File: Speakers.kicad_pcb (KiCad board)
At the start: 2 copper layers, 58.4 x 83.6 mm, 16 parts, among them J1 SR, J2 SL, J3 SAR, J4 SAL, J5 SBR, J6 SBL, J7 5V, Q1 S8050, Q2 S8050, U1 WeMos_mini

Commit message: Zmiana wartości R1 i R2
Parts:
- R1, R2: value 1k -> 1k8
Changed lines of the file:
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@@
       (effects (font (size 1 1) (thickness 0.15)) (justify mirror))
     )
-    (fp_text value 1k (at 0 -1.9 270) (layer B.Fab)
+    (fp_text value 1k8 (at 0 -1.9 270) (layer B.Fab)
       (effects (font (size 1 1) (thickness 0.15)) (justify mirror))
     )
@@
       (effects (font (size 1 1) (thickness 0.15)) (justify mirror))
     )
-    (fp_text value 1k (at 0 -1.9) (layer B.Fab)
+    (fp_text value 1k8 (at 0 -1.9) (layer B.Fab)
       (effects (font (size 1 1) (thickness 0.15)) (justify mirror))
     )
@@
   (segment (start 249.428 116.586) (end 240.792 107.95) (width 1.5) (layer B.Cu) (net 14))
   (segment (start 249.428 124.968) (end 249.428 116.586) (width 1.5) (layer B.Cu) (net 14))
-  (segment (start 228.092 103.632) (end 226.79 103.632) (width 1.5) (layer B.Cu) (net 14) (status 800000))
+  (segment (start 228.092 103.632) (end 226.79 103.632) (width 1.5) (layer B.Cu) (net 14))
   (segment (start 232.41 107.95) (end 228.092 103.632) (width 1.5) (layer B.Cu) (net 14))
-  (segment (start 230.312 97.766) (end 232.608 97.766) (width 1.5) (layer B.Cu) (net 15) (status C00000))
-  (segment (start 232.608 97.766) (end 232.664 97.822) (width 1.5) (layer B.Cu) (net 15) (status C00000))
+  (segment (start 230.312 97.766) (end 232.608 97.766) (width 1.5) (layer B.Cu) (net 15))
+  (segment (start 232.608 97.766) (end 232.664 97.822) (width 1.5) (layer B.Cu) (net 15))
   (segment (start 222.504 102.394) (end 222.504 98.552) (width 1.5) (layer B.Cu) (net 16))
   (segment (start 222.504 98.552) (end 222.25 98.298) (width 1.5) (layer B.Cu) (net 16))

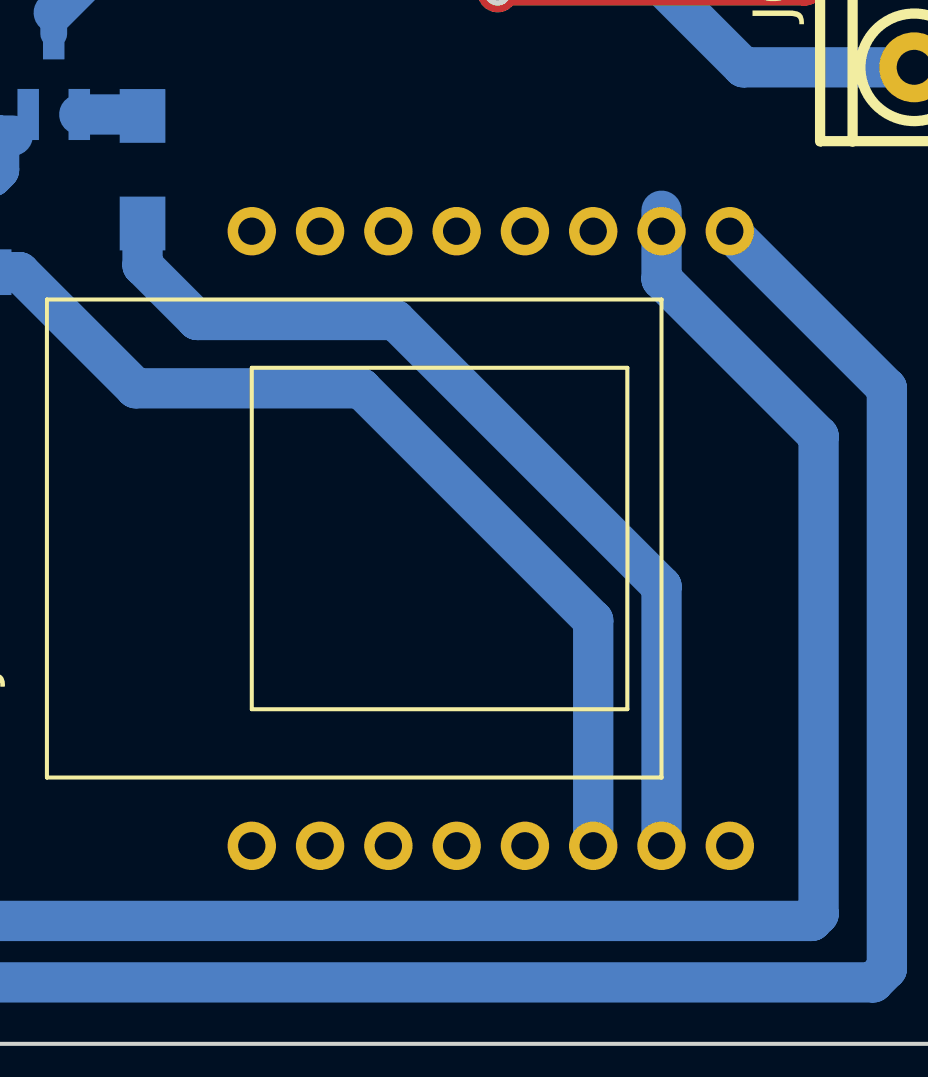
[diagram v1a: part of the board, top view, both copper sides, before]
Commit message: dodano plik pdf z PCB
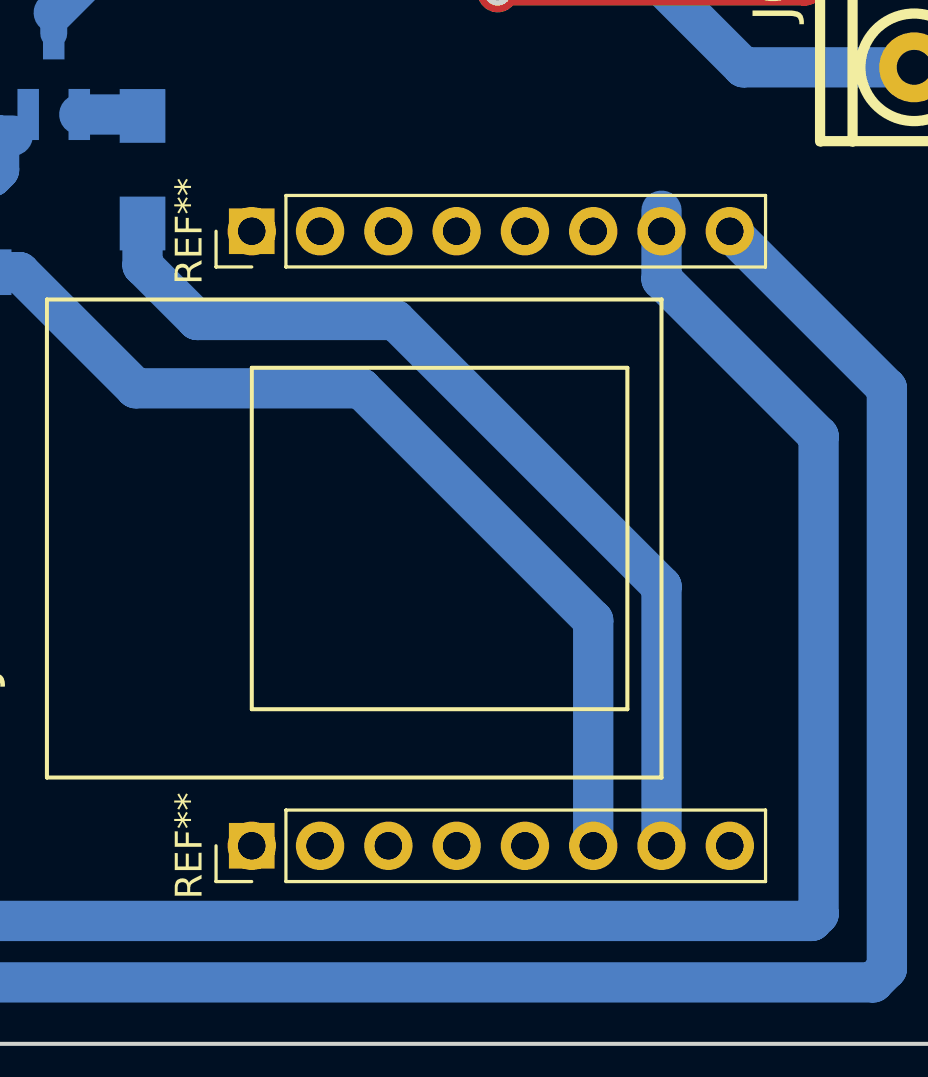
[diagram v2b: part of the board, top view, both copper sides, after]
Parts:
- added REF**: Socket_Strip_Straight_1x08_Pitch2.54mm, Socket_Strips:Socket_Strip_Straight_1x08_Pitch2.54mm, F.Cu at (236.7, 102.1)
- added REF**: Socket_Strip_Straight_1x08_Pitch2.54mm, Socket_Strips:Socket_Strip_Straight_1x08_Pitch2.54mm, F.Cu at (236.7, 125.0)
- R1, R2: value 1k8 -> 1k
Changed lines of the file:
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@@
-(kicad_pcb (version 4) (host pcbnew 4.0.7-e1-6374~58~ubuntu16.04.1)
+(kicad_pcb (version 4) (host pcbnew 4.0.7+dfsg1-1ubuntu2)
   (general
-    (links 30)
+    (links 0)
     (no_connects 2)
     (area 212.776999 48.692999 271.347001 132.409001)
@@
     (tracks 154)
     (zones 0)
-    (modules 16)
+    (modules 18)
     (nets 17)
   )
@@
     (pad_to_mask_clearance 0.2)
     (aux_axis_origin 0 0)
-    (visible_elements 7FFFFFFF)
+    (visible_elements 7FFFEFFF)
     (pcbplotparams
       (layerselection 0x00030_80000001)
@@
     (pad 14 thru_hole circle (at 25.32 0) (size 3 3) (drill 1.3) (layers *.Cu *.Mask)
       (net 7 "Net-(J5-Pad1)"))
-    (model ${KISYS3DMOD}/Relays_THT.3dshapes/Relay_DPDT_Finder_40.52.wrl
-      (at (xyz 0 0 0))
-      (scale (xyz 1 1 1))
-      (rotate (xyz 0 0 0))
+    (model Relays_THT.3dshapes/Rely_RM84.wrl
+      (at (xyz 1.06 0.1 0))
+      (scale (xyz 0.4 0.4 0.4))
+      (rotate (xyz 0 0 180))
     )
   )
@@
     (pad 14 thru_hole circle (at 25.32 0) (size 3 3) (drill 1.3) (layers *.Cu *.Mask)
       (net 7 "Net-(J5-Pad1)"))
-    (model ${KISYS3DMOD}/Relays_THT.3dshapes/Relay_DPDT_Finder_40.52.wrl
-      (at (xyz 0 0 0))
-      (scale (xyz 1 1 1))
-      (rotate (xyz 0 0 0))
+    (model Relays_THT.3dshapes/Rely_RM84.wrl
+      (at (xyz 1.06 0.1 0))
+      (scale (xyz 0.4 0.4 0.4))
+      (rotate (xyz 0 0 180))
     )
   )
@@
       (effects (font (size 1 1) (thickness 0.15)) (justify mirror))
     )
-    (fp_text value 1k8 (at 0 -1.9 270) (layer B.Fab)
+    (fp_text value 1k (at 0 -1.9 270) (layer B.Fab)
       (effects (font (size 1 1) (thickness 0.15)) (justify mirror))
     )
@@
       (effects (font (size 1 1) (thickness 0.15)) (justify mirror))
     )
-    (fp_text value 1k8 (at 0 -1.9) (layer B.Fab)
+    (fp_text value 1k (at 0 -1.9) (layer B.Fab)
       (effects (font (size 1 1) (thickness 0.15)) (justify mirror))
     )
@@
     )
   )
+  (module Socket_Strips:Socket_Strip_Straight_1x08_Pitch2.54mm (layer F.Cu)
+    (at 236.728 102.108 90)
+    (descr "Through hole straight socket strip, 1x08, 2.54mm pitch, single row")
+    (tags "Through hole socket strip THT 1x08 2.54mm single row")
+    (fp_text reference REF** (at 0 -2.33 90) (layer F.SilkS)
+      (effects (font (size 1 1) (thickness 0.15)))
+    )
+    (fp_text value Socket_Strip_Straight_1x08_Pitch2.54mm (at 0 20.11 90) (layer F.Fab)
+      (effects (font (size 1 1) (thickness 0.15)))
+    )
+    (fp_line (start -1.27 -1.27) (end -1.27 19.05) (layer F.Fab) (width 0.1))
+    (fp_line (start -1.27 19.05) (end 1.27 19.05) (layer F.Fab) (width 0.1))
+    (fp_line (start 1.27 19.05) (end 1.27 -1.27) (layer F.Fab) (width 0.1))
+    (fp_line (start 1.27 -1.27) (end -1.27 -1.27) (layer F.Fab) (width 0.1))
+    (fp_line (start -1.33 1.27) (end -1.33 19.11) (layer F.SilkS) (width 0.12))
+    (fp_line (start -1.33 19.11) (end 1.33 19.11) (layer F.SilkS) (width 0.12))
+    (fp_line (start 1.33 19.11) (end 1.33 1.27) (layer F.SilkS) (width 0.12))
+    (fp_line (start 1.33 1.27) (end -1.33 1.27) (layer F.SilkS) (width 0.12))
+    (fp_line (start -1.33 0) (end -1.33 -1.33) (layer F.SilkS) (width 0.12))
+    (fp_line (start -1.33 -1.33) (end 0 -1.33) (layer F.SilkS) (width 0.12))
+    (fp_line (start -1.8 -1.8) (end -1.8 19.55) (layer F.CrtYd) (width 0.05))
+    (fp_line (start -1.8 19.55) (end 1.8 19.55) (layer F.CrtYd) (width 0.05))
+    (fp_line (start 1.8 19.55) (end 1.8 -1.8) (layer F.CrtYd) (width 0.05))
+    (fp_line (start 1.8 -1.8) (end -1.8 -1.8) (layer F.CrtYd) (width 0.05))
+    (fp_text user %R (at 0 -2.33 90) (layer F.Fab)
+      (effects (font (size 1 1) (thickness 0.15)))
+    )
+    (pad 1 thru_hole rect (at 0 0 90) (size 1.7 1.7) (drill 1) (layers *.Cu *.Mask))
+    (pad 2 thru_hole oval (at 0 2.54 90) (size 1.7 1.7) (drill 1) (layers *.Cu *.Mask))
+    (pad 3 thru_hole oval (at 0 5.08 90) (size 1.7 1.7) (drill 1) (layers *.Cu *.Mask))
+    (pad 4 thru_hole oval (at 0 7.62 90) (size 1.7 1.7) (drill 1) (layers *.Cu *.Mask))
+    (pad 5 thru_hole oval (at 0 10.16 90) (size 1.7 1.7) (drill 1) (layers *.Cu *.Mask))
+    (pad 6 thru_hole oval (at 0 12.7 90) (size 1.7 1.7) (drill 1) (layers *.Cu *.Mask))
+    (pad 7 thru_hole oval (at 0 15.24 90) (size 1.7 1.7) (drill 1) (layers *.Cu *.Mask))
+    (pad 8 thru_hole oval (at 0 17.78 90) (size 1.7 1.7) (drill 1) (layers *.Cu *.Mask))
+    (model ${KISYS3DMOD}/Socket_Strips.3dshapes/Socket_Strip_Straight_1x08_Pitch2.54mm.wrl
+      (at (xyz 0 -0.35 0))
+      (scale (xyz 1 1 1))
+      (rotate (xyz 0 0 270))
+    )
+  )
+  (module Socket_Strips:Socket_Strip_Straight_1x08_Pitch2.54mm (layer F.Cu)
+    (at 236.728 124.968 90)
+    (descr "Through hole straight socket strip, 1x08, 2.54mm pitch, single row")
+    (tags "Through hole socket strip THT 1x08 2.54mm single row")
+    (fp_text reference REF** (at 0 -2.33 90) (layer F.SilkS)
+      (effects (font (size 1 1) (thickness 0.15)))
+    )
+    (fp_text value Socket_Strip_Straight_1x08_Pitch2.54mm (at 0 20.11 90) (layer F.Fab)
+      (effects (font (size 1 1) (thickness 0.15)))
+    )
+    (fp_line (start -1.27 -1.27) (end -1.27 19.05) (layer F.Fab) (width 0.1))
+    (fp_line (start -1.27 19.05) (end 1.27 19.05) (layer F.Fab) (width 0.1))
+    (fp_line (start 1.27 19.05) (end 1.27 -1.27) (layer F.Fab) (width 0.1))
+    (fp_line (start 1.27 -1.27) (end -1.27 -1.27) (layer F.Fab) (width 0.1))
+    (fp_line (start -1.33 1.27) (end -1.33 19.11) (layer F.SilkS) (width 0.12))
+    (fp_line (start -1.33 19.11) (end 1.33 19.11) (layer F.SilkS) (width 0.12))
+    (fp_line (start 1.33 19.11) (end 1.33 1.27) (layer F.SilkS) (width 0.12))
+    (fp_line (start 1.33 1.27) (end -1.33 1.27) (layer F.SilkS) (width 0.12))
+    (fp_line (start -1.33 0) (end -1.33 -1.33) (layer F.SilkS) (width 0.12))
+    (fp_line (start -1.33 -1.33) (end 0 -1.33) (layer F.SilkS) (width 0.12))
+    (fp_line (start -1.8 -1.8) (end -1.8 19.55) (layer F.CrtYd) (width 0.05))
+    (fp_line (start -1.8 19.55) (end 1.8 19.55) (layer F.CrtYd) (width 0.05))
+    (fp_line (start 1.8 19.55) (end 1.8 -1.8) (layer F.CrtYd) (width 0.05))
+    (fp_line (start 1.8 -1.8) (end -1.8 -1.8) (layer F.CrtYd) (width 0.05))
+    (fp_text user %R (at 0 -2.33 90) (layer F.Fab)
+      (effects (font (size 1 1) (thickness 0.15)))
+    )
+    (pad 1 thru_hole rect (at 0 0 90) (size 1.7 1.7) (drill 1) (layers *.Cu *.Mask))
+    (pad 2 thru_hole oval (at 0 2.54 90) (size 1.7 1.7) (drill 1) (layers *.Cu *.Mask))
+    (pad 3 thru_hole oval (at 0 5.08 90) (size 1.7 1.7) (drill 1) (layers *.Cu *.Mask))
+    (pad 4 thru_hole oval (at 0 7.62 90) (size 1.7 1.7) (drill 1) (layers *.Cu *.Mask))
+    (pad 5 thru_hole oval (at 0 10.16 90) (size 1.7 1.7) (drill 1) (layers *.Cu *.Mask))
+    (pad 6 thru_hole oval (at 0 12.7 90) (size 1.7 1.7) (drill 1) (layers *.Cu *.Mask))
+    (pad 7 thru_hole oval (at 0 15.24 90) (size 1.7 1.7) (drill 1) (layers *.Cu *.Mask))
+    (pad 8 thru_hole oval (at 0 17.78 90) (size 1.7 1.7) (drill 1) (layers *.Cu *.Mask))
+    (model ${KISYS3DMOD}/Socket_Strips.3dshapes/Socket_Strip_Straight_1x08_Pitch2.54mm.wrl
+      (at (xyz 0 -0.35 0))
+      (scale (xyz 1 1 1))
+      (rotate (xyz 0 0 270))
+    )
+  )

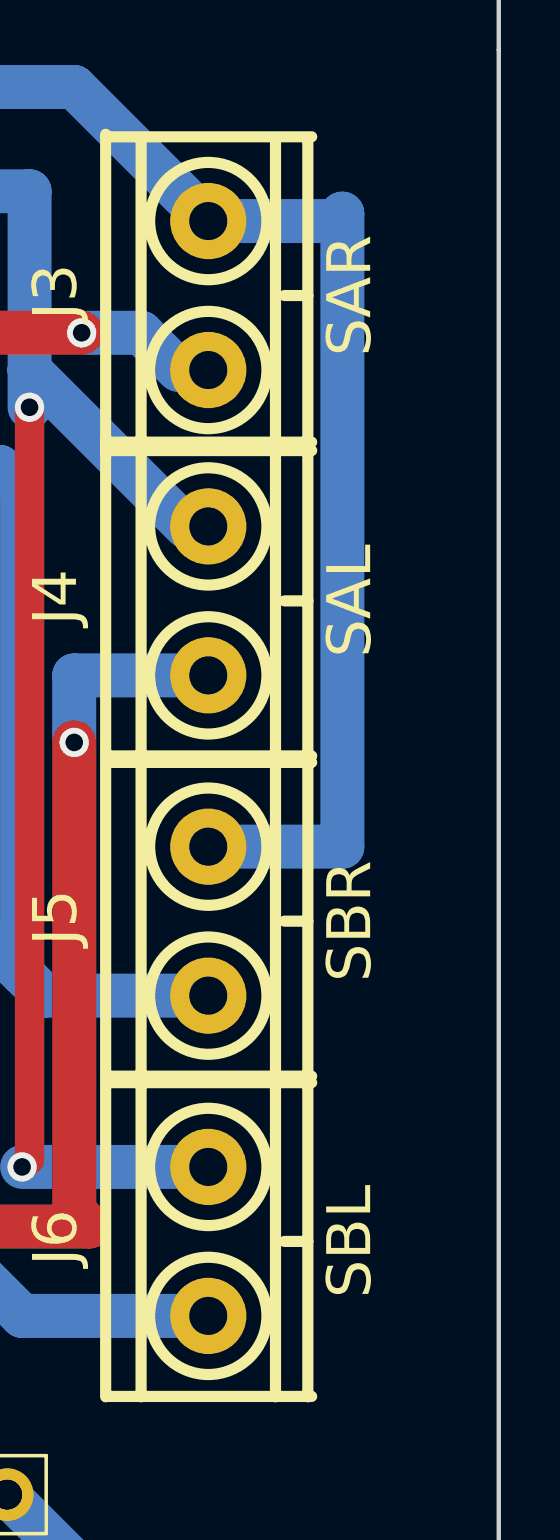
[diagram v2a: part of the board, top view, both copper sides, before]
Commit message: dodano opisy przy złączkach na warstwie górnej
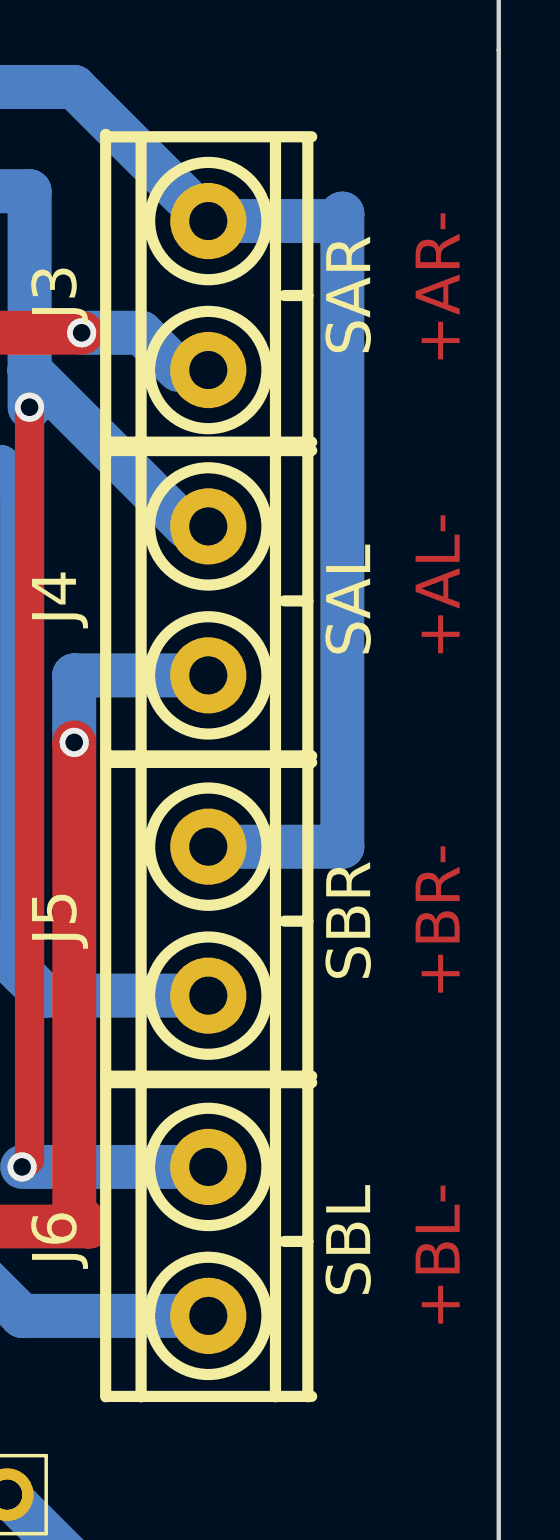
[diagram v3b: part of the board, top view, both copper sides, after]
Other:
- board text added: "+AL-"
- board text added: "+AR-"
- board text added: "+BL-"
- board text added: "+BR-"
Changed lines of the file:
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@@
 (kicad_pcb (version 4) (host pcbnew 4.0.7+dfsg1-1ubuntu2)
   (general
-    (links 0)
+    (links 30)
     (no_connects 2)
     (area 212.776999 48.692999 271.347001 132.409001)
     (thickness 1.6)
-    (drawings 16)
+    (drawings 20)
     (tracks 154)
     (zones 0)
@@
     )
   )
+  (gr_text +AR- (at 269.24 60.96 90) (layer F.Cu)
+    (effects (font (size 1.5 1.5) (thickness 0.3)))
+  )
+  (gr_text +AL- (at 269.24 71.12 90) (layer F.Cu)
+    (effects (font (size 1.5 1.5) (thickness 0.3)))
+  )
+  (gr_text +BR- (at 269.24 82.55 90) (layer F.Cu)
+    (effects (font (size 1.5 1.5) (thickness 0.3)))
+  )
+  (gr_text +BL- (at 269.24 93.98 90) (layer F.Cu)
+    (effects (font (size 1.5 1.5) (thickness 0.3)))
+  )
   (gr_line (start 212.852 132.334) (end 212.852 130.048) (angle 90) (layer Edge.Cuts) (width 0.15))
